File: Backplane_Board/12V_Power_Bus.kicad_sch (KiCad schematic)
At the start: 17 parts

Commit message: ready for final schmatic review
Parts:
- renumbered 10k to 10k1
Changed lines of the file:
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@@
 		(dnp no)
 		(fields_autoplaced yes)
-		(property "Reference" "10k"
+		(property "Reference" "10k1"
 			(at 137.16 64.7699 0)
 			(effects
@@
 			(project "Backplane_Board"
 				(path "/4484cfee-9e43-4cef-88b4-a8ca308542b4/7cc9cec9-7faa-4853-bd66-b7a2d884c738"
-					(reference "10k")
+					(reference "10k1")
 					(unit 1)
 				)

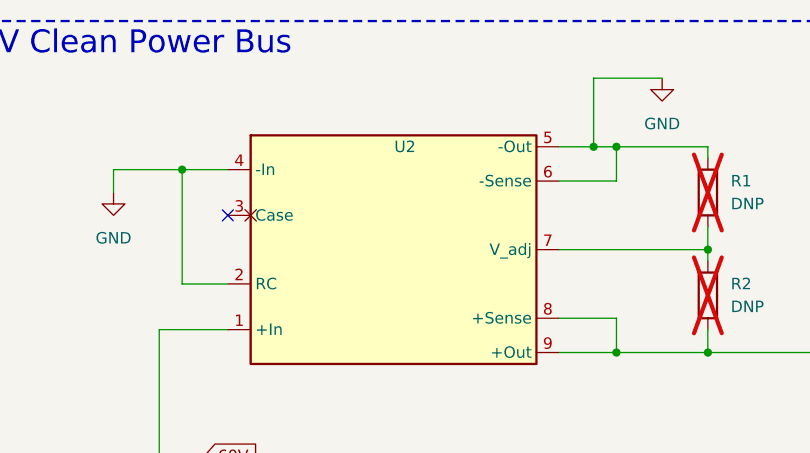
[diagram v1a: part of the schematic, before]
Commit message: updated i2c pullups to 3V3 logic, not isolator needed
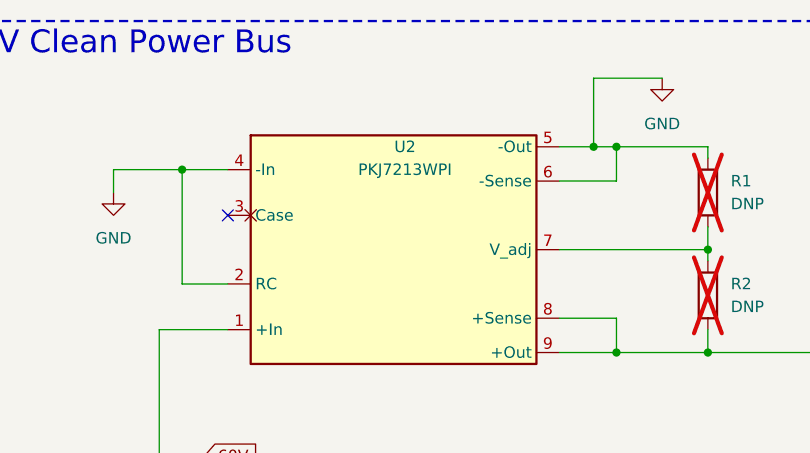
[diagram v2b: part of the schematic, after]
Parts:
- U2: value ~ -> PKJ7213WPI
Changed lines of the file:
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@@
+	)
+	(symbol
+		(lib_id "PKJ7213WPI:PKJ7213WPI")
+		(at 71.12 38.1 0)
+		(unit 1)
+		(exclude_from_sim no)
+		(in_bom yes)
+		(on_board yes)
+		(dnp no)
+		(fields_autoplaced yes)
+		(property "Reference" "U2"
+			(at 71.755 26.67 0)
+			(effects
+				(font
+					(size 1.27 1.27)
+				)
+			)
+		)
+		(property "Value" "PKJ7213WPI"
+			(at 71.755 29.21 0)
+			(effects
+				(font
+					(size 1.27 1.27)
+				)
+			)
+		)
+		(property "Footprint" ""
+			(at 71.12 38.1 0)
+			(effects
+				(font
+					(size 1.27 1.27)
+				)
+				(hide yes)
+			)
+		)
+		(property "Datasheet" "https://flexpowermodules.com/resources/fpm-techspec-pkj7200w"
+			(at 71.12 38.1 0)
+			(effects
+				(font
+					(size 1.27 1.27)
+				)
+				(hide yes)
+			)
+		)
+		(property "Description" "PKJ 7200W series DC-DC Converters Input 14-160 V, Output up to 16.7 A / 200 W"
+			(at 71.12 38.1 0)
+			(effects
+				(font
+					(size 1.27 1.27)
+				)
+				(hide yes)
+			)
+		)
+		(pin "8"
+		)
+		(pin "2"
+		)
+		(pin "1"
+		)
+		(pin "5"
+		)
+		(pin "6"
+		)
+		(pin "7"
+		)
+		(pin "4"
+		)
+		(pin "3"
+		)
+		(pin "9"
+		)
+		(instances
+			(project "Backplane_Board"
+				(path "/4484cfee-9e43-4cef-88b4-a8ca308542b4/7cc9cec9-7faa-4853-bd66-b7a2d884c738"
+					(reference "U2")
+					(unit 1)
+				)
+			)
+		)
 	)
 	(symbol
@@
 					(unit 1)
 				)
-			)
-		)
-	)
-	(symbol
-		(lib_id "PKJ7213WPI:PKJ7213WPI")
-		(at 71.12 38.1 0)
-		(unit 1)
-		(exclude_from_sim no)
-		(in_bom yes)
-		(on_board yes)
-		(dnp no)
-		(fields_autoplaced yes)
-		(property "Reference" "U2"
-			(at 71.755 26.67 0)
-			(effects
-				(font
-					(size 1.27 1.27)
-				)
-			)
-		)
-		(property "Value" "~"
-			(at 71.755 29.21 0)
-			(effects
-				(font
-					(size 1.27 1.27)
-				)
-			)
-		)
-		(property "Footprint" ""
-			(at 71.12 38.1 0)
-			(effects
-				(font
-					(size 1.27 1.27)
-				)
-				(hide yes)
-			)
-		)
-		(property "Datasheet" ""
-			(at 71.12 38.1 0)
-			(effects
-				(font
-					(size 1.27 1.27)
-				)
-				(hide yes)
-			)
-		)
-		(property "Description" ""
-			(at 71.12 38.1 0)
-			(effects
-				(font
-					(size 1.27 1.27)
-				)
-				(hide yes)
-			)
-		)
-		(pin "8"
-		)
-		(pin "2"
-		)
-		(pin "1"
-		)
-		(pin "5"
-		)
-		(pin "6"
-		)
-		(pin "7"
-		)
-		(pin "4"
-		)
-		(pin "3"
-		)
-		(pin "9"
-		)
-		(instances
-			(project "Backplane_Board"
-				(path "/4484cfee-9e43-4cef-88b4-a8ca308542b4/7cc9cec9-7faa-4853-bd66-b7a2d884c738"
-					(reference "U2")
-					(unit 1)
-				)

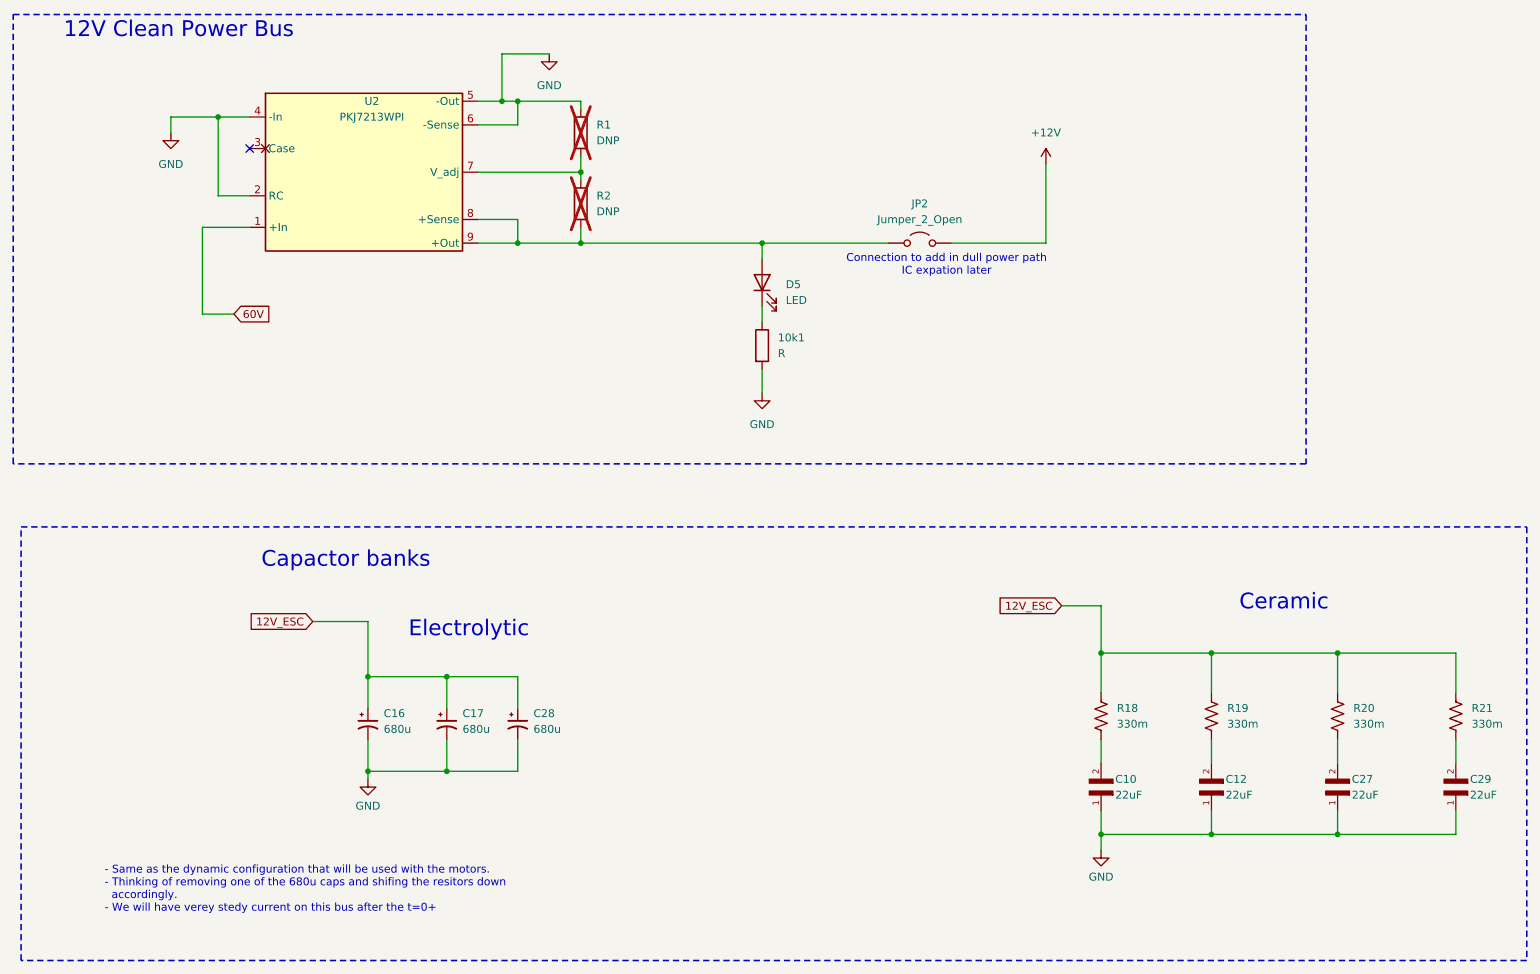
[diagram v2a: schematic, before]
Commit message: update FET circits
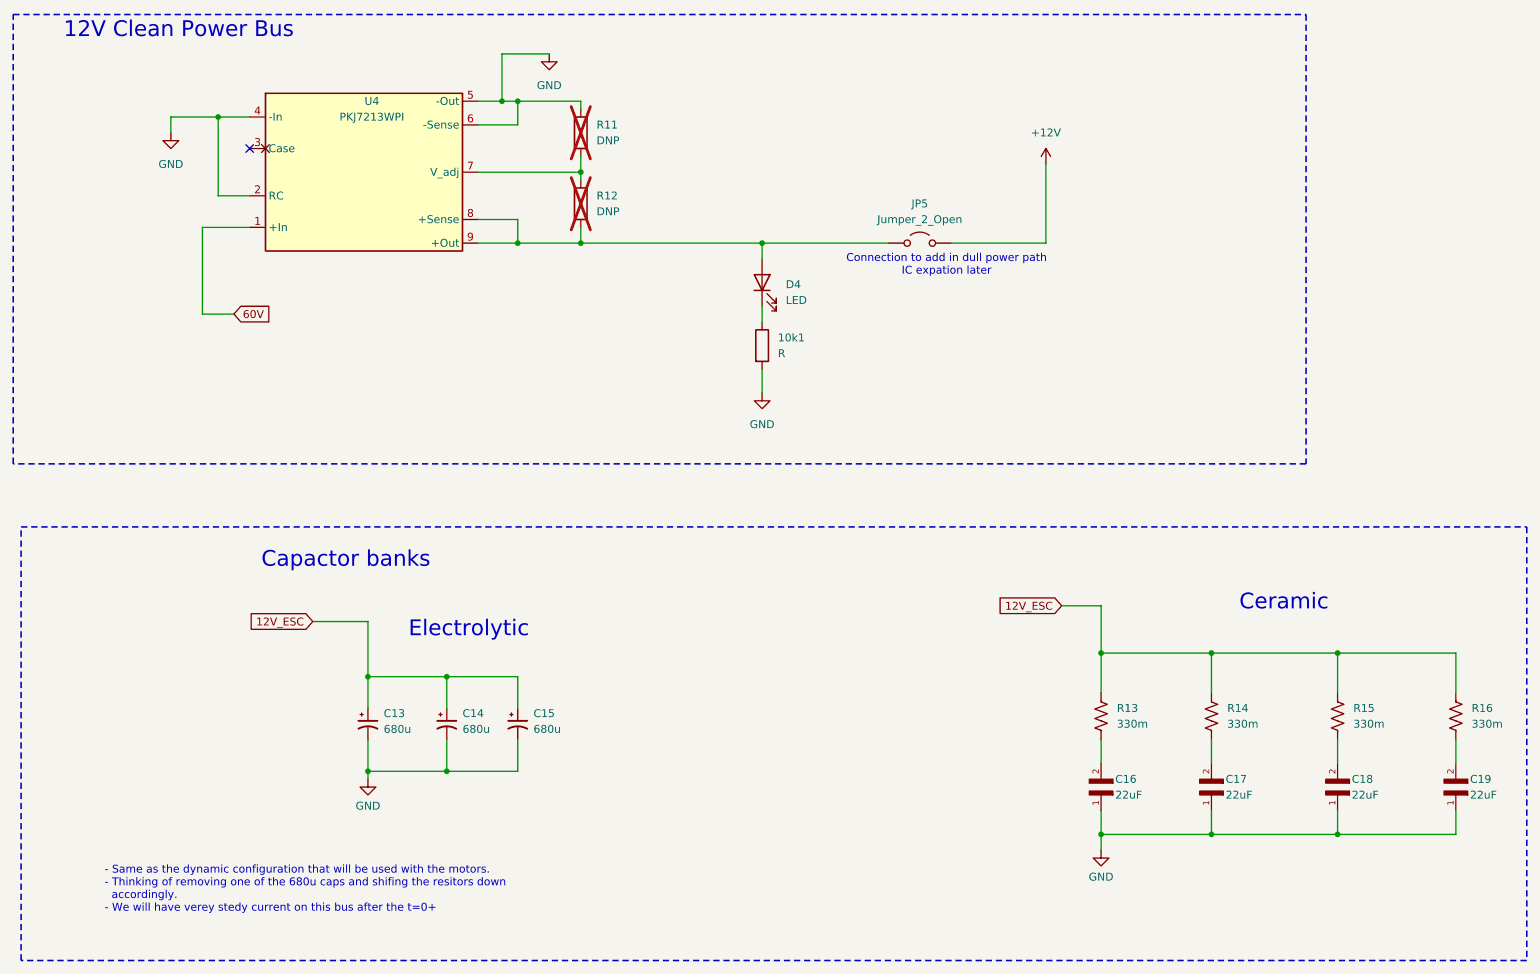
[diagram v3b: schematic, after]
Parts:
- U4: renamed from U2; footprint (none) -> Library:PKJ7213WPI
- renumbered C16 to C13, C17 to C14, C28 to C15, C10 to C16, C12 to C17, C27 to C18, C29 to C19, D5 to D4, JP2 to JP5, R1 to R11, R2 to R12, R18 to R13, R19 to R14, R20 to R15, R21 to R16
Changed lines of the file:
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@@
 		(dnp no)
 		(fields_autoplaced yes)
-		(property "Reference" "C16"
+		(property "Reference" "C13"
 			(at 73.66 125.2981 0)
 			(effects
@@
 			(project "Backplane_Board"
 				(path "/4484cfee-9e43-4cef-88b4-a8ca308542b4/7cc9cec9-7faa-4853-bd66-b7a2d884c738"
-					(reference "C16")
+					(reference "C13")
 					(unit 1)
 				)
@@
 		(dnp no)
 		(fields_autoplaced yes)
-		(property "Reference" "C28"
+		(property "Reference" "C15"
 			(at 97.79 125.2981 0)
 			(effects
@@
 			(project "Backplane_Board"
 				(path "/4484cfee-9e43-4cef-88b4-a8ca308542b4/7cc9cec9-7faa-4853-bd66-b7a2d884c738"
-					(reference "C28")
+					(reference "C15")
 					(unit 1)
 				)
@@
 		(dnp no)
 		(fields_autoplaced yes)
-		(property "Reference" "#PWR013"
+		(property "Reference" "#PWR026"
 			(at 134.62 80.01 0)
 			(effects
@@
 			(project "Backplane_Board"
 				(path "/4484cfee-9e43-4cef-88b4-a8ca308542b4/7cc9cec9-7faa-4853-bd66-b7a2d884c738"
-					(reference "#PWR013")
+					(reference "#PWR026")
 					(unit 1)
 				)
@@
 		(dnp no)
 		(fields_autoplaced yes)
-		(property "Reference" "U2"
+		(property "Reference" "U4"
 			(at 71.755 26.67 0)
 			(effects
@@
 			)
 		)
-		(property "Footprint" ""
+		(property "Footprint" "Library:PKJ7213WPI"
 			(at 71.12 38.1 0)
 			(effects
@@
 			(project "Backplane_Board"
 				(path "/4484cfee-9e43-4cef-88b4-a8ca308542b4/7cc9cec9-7faa-4853-bd66-b7a2d884c738"
-					(reference "U2")
+					(reference "U4")
 					(unit 1)
 				)
@@
 		(dnp no)
 		(fields_autoplaced yes)
-		(property "Reference" "JP2"
+		(property "Reference" "JP5"
 			(at 160.02 43.18 0)
 			(effects
@@
 			(project "Backplane_Board"
 				(path "/4484cfee-9e43-4cef-88b4-a8ca308542b4/7cc9cec9-7faa-4853-bd66-b7a2d884c738"
-					(reference "JP2")
+					(reference "JP5")
 					(unit 1)
 				)
@@
 		(on_board yes)
 		(dnp no)
-		(property "Reference" "#PWR028"
+		(property "Reference" "#PWR027"
 			(at 71.12 142.24 0)
 			(effects
@@
 			(project "Backplane_Board"
 				(path "/4484cfee-9e43-4cef-88b4-a8ca308542b4/7cc9cec9-7faa-4853-bd66-b7a2d884c738"
-					(reference "#PWR028")
+					(reference "#PWR027")
 					(unit 1)
 				)
@@
 		(on_board yes)
 		(dnp no)
-		(property "Reference" "C29"
+		(property "Reference" "C19"
 			(at 248.666 135.89 90)
 			(effects
@@
 			(project "Backplane_Board"
 				(path "/4484cfee-9e43-4cef-88b4-a8ca308542b4/7cc9cec9-7faa-4853-bd66-b7a2d884c738"
-					(reference "C29")
+					(reference "C19")
 					(unit 1)
 				)
@@
 		(dnp no)
 		(fields_autoplaced yes)
-		(property "Reference" "#PWR02"
+		(property "Reference" "#PWR023"
 			(at 100.33 25.4 0)
 			(effects
@@
 			(project "Backplane_Board"
 				(path "/4484cfee-9e43-4cef-88b4-a8ca308542b4/7cc9cec9-7faa-4853-bd66-b7a2d884c738"
-					(reference "#PWR02")
+					(reference "#PWR023")
 					(unit 1)
 				)
@@
 		(dnp no)
 		(fields_autoplaced yes)
-		(property "Reference" "C17"
+		(property "Reference" "C14"
 			(at 86.36 125.2981 0)
 			(effects
@@
 			(project "Backplane_Board"
 				(path "/4484cfee-9e43-4cef-88b4-a8ca308542b4/7cc9cec9-7faa-4853-bd66-b7a2d884c738"
-					(reference "C17")
+					(reference "C14")
 					(unit 1)
 				)
@@
 		(dnp no)
 		(fields_autoplaced yes)
-		(property "Reference" "R18"
+		(property "Reference" "R13"
 			(at 191.77 124.4599 0)
 			(effects
@@
 			(project "Backplane_Board"
 				(path "/4484cfee-9e43-4cef-88b4-a8ca308542b4/7cc9cec9-7faa-4853-bd66-b7a2d884c738"
-					(reference "R18")
+					(reference "R13")
 					(unit 1)
 				)
@@
 		(on_board yes)
 		(dnp no)
-		(property "Reference" "C12"
+		(property "Reference" "C17"
 			(at 209.296 135.89 90)
 			(effects
@@
 			(project "Backplane_Board"
 				(path "/4484cfee-9e43-4cef-88b4-a8ca308542b4/7cc9cec9-7faa-4853-bd66-b7a2d884c738"
-					(reference "C12")
+					(reference "C17")
 					(unit 1)
 				)
@@
 		(dnp no)
 		(fields_autoplaced yes)
-		(property "Reference" "#PWR05"
+		(property "Reference" "#PWR024"
 			(at 39.37 38.1 0)
 			(effects
@@
 			(project "Backplane_Board"
 				(path "/4484cfee-9e43-4cef-88b4-a8ca308542b4/7cc9cec9-7faa-4853-bd66-b7a2d884c738"
-					(reference "#PWR05")
+					(reference "#PWR024")
 					(unit 1)
 				)
@@
 		(on_board yes)
 		(dnp no)
-		(property "Reference" "C10"
+		(property "Reference" "C16"
 			(at 191.516 135.89 90)
 			(effects
@@
 			(project "Backplane_Board"
 				(path "/4484cfee-9e43-4cef-88b4-a8ca308542b4/7cc9cec9-7faa-4853-bd66-b7a2d884c738"
-					(reference "C10")
+					(reference "C16")
 					(unit 1)
 				)
@@
 		(on_board yes)
 		(dnp no)
-		(property "Reference" "#PWR027"
+		(property "Reference" "#PWR028"
 			(at 189.23 153.67 0)
 			(effects
@@
 			(project "Backplane_Board"
 				(path "/4484cfee-9e43-4cef-88b4-a8ca308542b4/7cc9cec9-7faa-4853-bd66-b7a2d884c738"
-					(reference "#PWR027")
+					(reference "#PWR028")
 					(unit 1)
 				)
@@
 		(dnp no)
 		(fields_autoplaced yes)
-		(property "Reference" "D5"
+		(property "Reference" "D4"
 			(at 138.43 56.1974 90)
 			(effects
@@
 			(project "Backplane_Board"
 				(path "/4484cfee-9e43-4cef-88b4-a8ca308542b4/7cc9cec9-7faa-4853-bd66-b7a2d884c738"
-					(reference "D5")
+					(reference "D4")
 					(unit 1)
 				)
@@
 		(dnp yes)
 		(fields_autoplaced yes)
-		(property "Reference" "R2"
+		(property "Reference" "R12"
 			(at 107.95 41.9099 0)
 			(effects
@@
 			(project "Backplane_Board"
 				(path "/4484cfee-9e43-4cef-88b4-a8ca308542b4/7cc9cec9-7faa-4853-bd66-b7a2d884c738"
-					(reference "R2")
+					(reference "R12")
 					(unit 1)
 				)
@@
 		(dnp no)
 		(fields_autoplaced yes)
-		(property "Reference" "#PWR01"
+		(property "Reference" "#PWR025"
 			(at 180.34 40.64 0)
 			(effects
@@
 			(project "Backplane_Board"
 				(path "/4484cfee-9e43-4cef-88b4-a8ca308542b4/7cc9cec9-7faa-4853-bd66-b7a2d884c738"
-					(reference "#PWR01")
+					(reference "#PWR025")
 					(unit 1)
 				)
@@
 		(on_board yes)
 		(dnp no)
-		(property "Reference" "C27"
+		(property "Reference" "C18"
 			(at 229.616 135.89 90)
 			(effects
@@
 			(project "Backplane_Board"
 				(path "/4484cfee-9e43-4cef-88b4-a8ca308542b4/7cc9cec9-7faa-4853-bd66-b7a2d884c738"
-					(reference "C27")
+					(reference "C18")
 					(unit 1)
 				)
@@
 		(dnp no)
 		(fields_autoplaced yes)
-		(property "Reference" "R20"
+		(property "Reference" "R15"
 			(at 229.87 124.4599 0)
 			(effects
@@
 			(project "Backplane_Board"
 				(path "/4484cfee-9e43-4cef-88b4-a8ca308542b4/7cc9cec9-7faa-4853-bd66-b7a2d884c738"
-					(reference "R20")
+					(reference "R15")
 					(unit 1)
 				)
@@
 		(dnp no)
 		(fields_autoplaced yes)
-		(property "Reference" "R21"
+		(property "Reference" "R16"
 			(at 248.92 124.4599 0)
 			(effects
@@
 			(project "Backplane_Board"
 				(path "/4484cfee-9e43-4cef-88b4-a8ca308542b4/7cc9cec9-7faa-4853-bd66-b7a2d884c738"
-					(reference "R21")
+					(reference "R16")
 					(unit 1)
 				)
@@
 		(dnp yes)
 		(fields_autoplaced yes)
-		(property "Reference" "R1"
+		(property "Reference" "R11"
 			(at 107.95 30.4799 0)
 			(effects
@@
 			(project "Backplane_Board"
 				(path "/4484cfee-9e43-4cef-88b4-a8ca308542b4/7cc9cec9-7faa-4853-bd66-b7a2d884c738"
-					(reference "R1")
+					(reference "R11")
 					(unit 1)
 				)
@@
 		(dnp no)
 		(fields_autoplaced yes)
-		(property "Reference" "R19"
+		(property "Reference" "R14"
 			(at 209.55 124.4599 0)
 			(effects
@@
 			(project "Backplane_Board"
 				(path "/4484cfee-9e43-4cef-88b4-a8ca308542b4/7cc9cec9-7faa-4853-bd66-b7a2d884c738"
-					(reference "R19")
-					(unit 1)
-				)
+					(reference "R14")
+					(unit 1)
+				)
